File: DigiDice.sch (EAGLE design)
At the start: 29 parts, among them IC1 MCP6282-E/SN-ND, SW1 SPST_SWITCH, SW2 SPST_SWITCH, SW3 SPST_SWITCH, SW4 SPST_SWITCH, SW5 SPST_SWITCH, SW6 SPST_SWITCH, U1 ATMEGA168

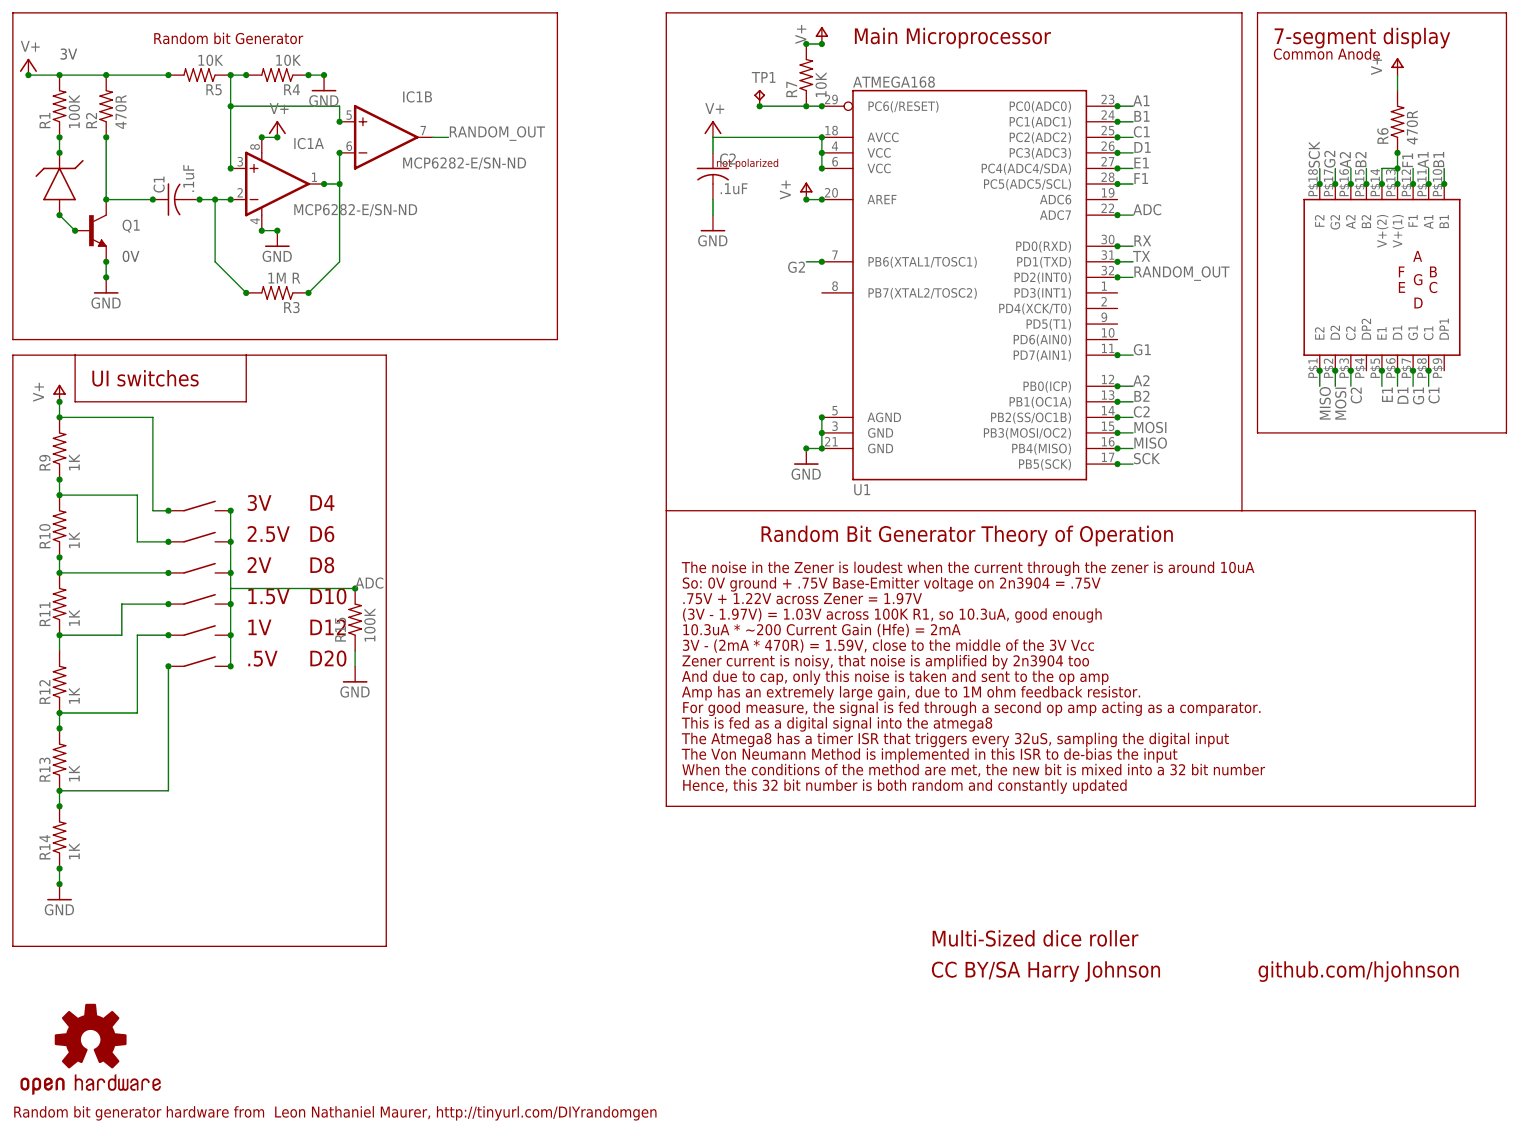
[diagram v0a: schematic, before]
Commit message: MAJOR COMMIT: New Version of Project
Officially Renamed to DigiDice, produced by kippkitts (kippkitts.com)
Changed board layout to remove need for power switch, hearty change in
code to accompany, now only 2.4-2.8mA quiescent.
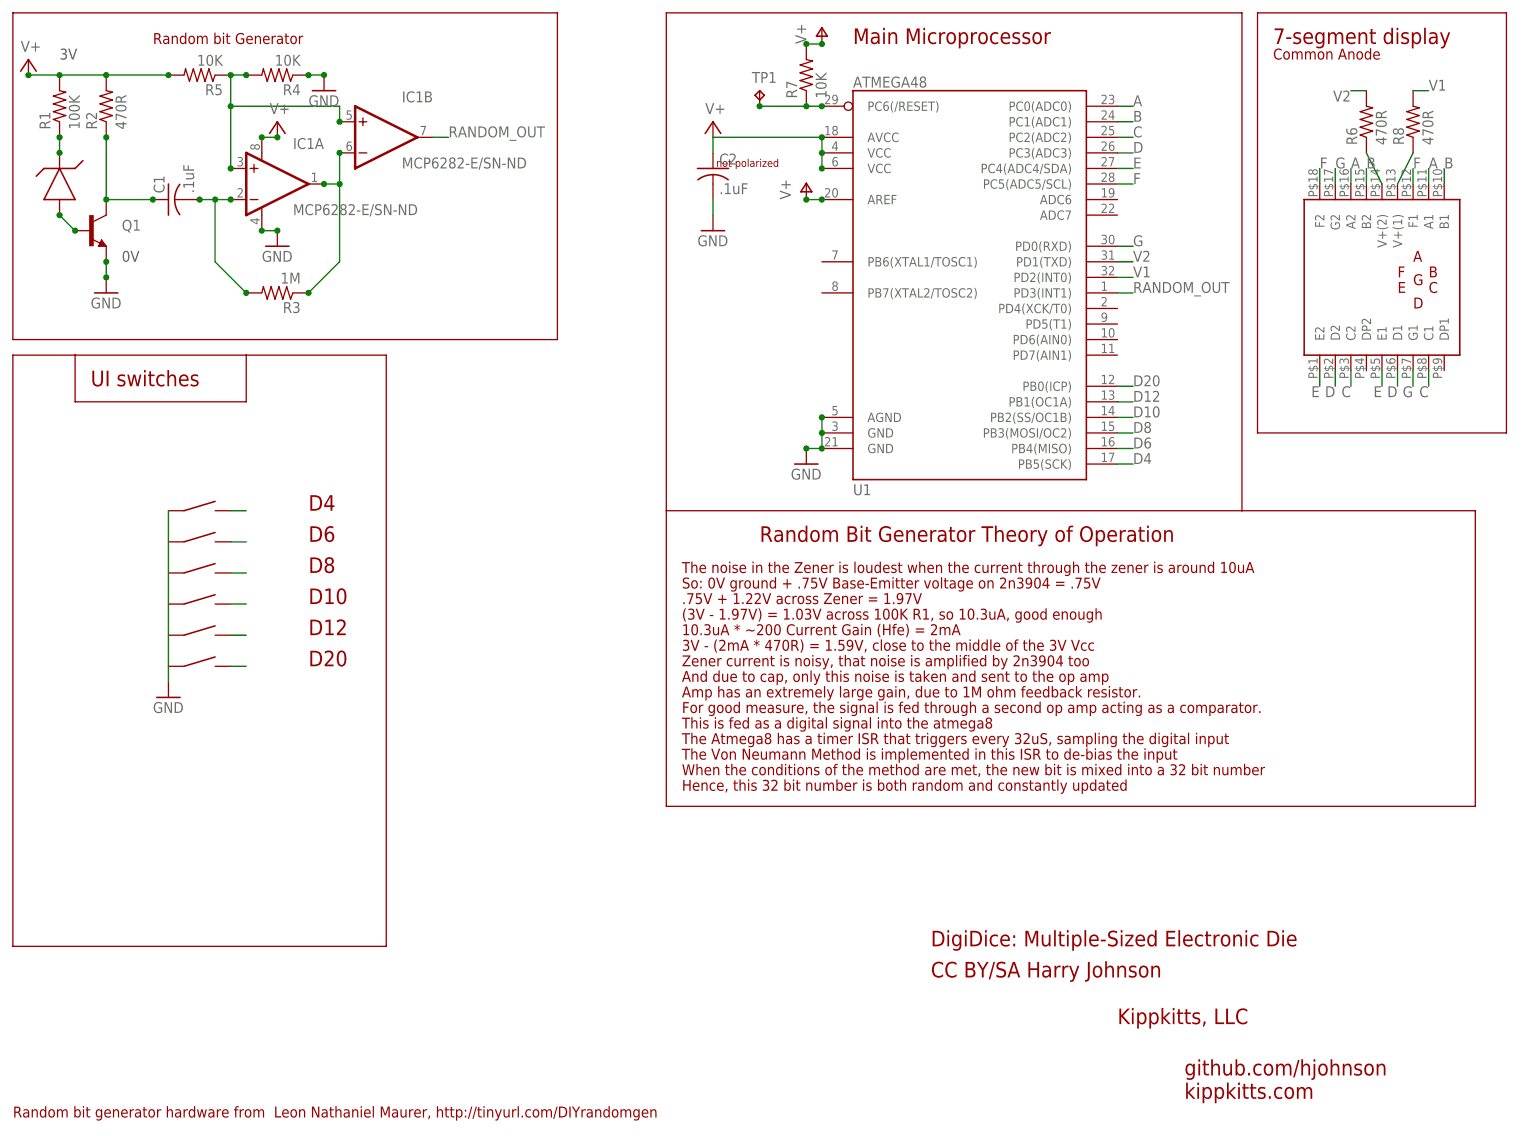
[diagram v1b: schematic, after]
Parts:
- removed R10, R11, R12, R13, R14, R9: 1K, adafruit:R-US_R0805
- removed R15: 100K, adafruit:R-US_R0805
- removed U$3: OSHW-LOGOS, SparkFun:OSHW-LOGOS
- added R8: 470R, adafruit:R-US_R0805
- R3: value 1M R -> 1M; device SparkFun:RESISTOR0805-RES -> adafruit:R-US_R0805
- U1: value ATMEGA168 -> ATMEGA48
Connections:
- removed net A1: U$2.A1, U1.PC0(ADC0)
- removed net A2: U$2.A2, U1.PB0(ICP)
- removed net ADC: R15.2, SW1.2, SW2.2, SW3.2, SW4.2, SW5.2, SW6.2, U1.ADC7
- removed net B1: U$2.B1, U1.PC1(ADC1)
- removed net B2: U$2.B2, U1.PB1(OC1A)
- removed net C1: U$2.C1, U1.PC2(ADC2)
- removed net C2: U$2.C2, U1.PB2(SS/OC1B)
- removed net D1: U$2.D1, U1.PC3(ADC3)
- removed net E1: U$2.E1, U1.PC4(ADC4/SDA)
- removed net F1: U$2.F1, U1.PC5(ADC5/SCL)
- removed net G1: U$2.G1, U1.PD7(AIN1)
- removed net G2: U$2.G2, U1.PB6(XTAL1/TOSC1)
- removed net MISO: U$2.E2, U1.PB4(MISO)
- removed net MOSI: U$2.D2, U1.PB3(MOSI/OC2)
- removed net N$11: R6.1, U$2.V+(1), U$2.V+(2)
- removed net ROLL_D10: R11.1, R12.2, SW4.1
- removed net ROLL_D12: R12.1, R13.2, SW5.1
- removed net ROLL_D20: R13.1, R14.2, SW6.1
- removed net ROLL_D6: R10.2, R9.1, SW2.1
- removed net ROLL_D8: R10.1, R11.2, SW3.1
- removed net RX: U1.PD0(RXD)
- removed net SCK: U$2.F2, U1.PB5(SCK)
- removed net TX: U1.PD1(TXD)
- new net A: U$2.A1, U$2.A2, U1.PC0(ADC0)
- new net B: U$2.B1, U$2.B2, U1.PC1(ADC1)
- new net C: U$2.C1, U$2.C2, U1.PC2(ADC2)
- new net D: U$2.D1, U$2.D2, U1.PC3(ADC3)
- new net D10: SW4.2, U1.PB2(SS/OC1B)
- new net D12: SW5.2, U1.PB1(OC1A)
- new net D20: SW6.2, U1.PB0(ICP)
- new net D4: SW1.2, U1.PB5(SCK)
- new net D6: SW2.2, U1.PB4(MISO)
- new net D8: SW3.2, U1.PB3(MOSI/OC2)
- new net E: U$2.E1, U$2.E2, U1.PC4(ADC4/SDA)
- new net F: U$2.F1, U$2.F2, U1.PC5(ADC5/SCL)
- new net G: U$2.G1, U$2.G2, U1.PD0(RXD)
- new net V1: R8.2, U1.PD2(INT0)
- new net V1_LED: R8.1, U$2.V+(1)
- new net V2: R6.2, U1.PD1(TXD)
- new net V2_LED: R6.1, U$2.V+(2)
- net GND: now also SW1.1, SW2.1, SW3.1, SW4.1, SW5.1, SW6.1; no longer R14.1, R15.1
- net RANDOM_OUT: now also U1.PD3(INT1); no longer U1.PD2(INT0)
- net V+: no longer R6.2, R9.2, SW1.1
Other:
- note added: "DigiDice: Multiple-Sized Electronic Die"
- note added: "Kippkitts, LLC"
- note added: "kippkitts.com"
- note removed: ".5V"
- note removed: "1.5V"
- note removed: "1V"
- note removed: "2.5V"
- note removed: "2V"
- note removed: "Multi-Sized dice roller"
- moved on the sheet: R6
